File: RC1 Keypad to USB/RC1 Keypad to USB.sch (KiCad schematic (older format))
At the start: 7 parts, among them J1 RC1 Keypad Port, SW1 RESET

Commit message: Assigned keypad adapter footprints
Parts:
- A1: footprint (none) -> Arduino_Pro_Micro:Arduino_Pro_Micro
- D1, D2: renamed from D?; footprint (none) -> LEDs:LED_D5.0mm
- J1: footprint (none) -> Pin_Headers:Pin_Header_Straight_2x08_Pitch2.54mm
- R1, R2: renamed from R?; footprint (none) -> Resistors_THT:R_Axial_DIN0207_L6.3mm_D2.5mm_P10.16mm_Horizontal
- SW1: footprint (none) -> Buttons_Switches_THT:SW_PUSH_6mm
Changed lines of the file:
@@
 F 0 "J1" H 3975 3700 50  0000 C CNN
 F 1 "RC1 Keypad Port" H 4250 2500 50  0000 C CNN
-F 2 "" H 4200 3300 50  0001 C CNN
+F 2 "Pin_Headers:Pin_Header_Straight_2x08_Pitch2.54mm" H 4200 3300 50  0001 C CNN
 F 3 "" H 4200 3300 50  0001 C CNN
 	1    4250 3300
@@
 F 0 "A1" H 6350 3675 50  0000 C CNN
 F 1 "Arduino Pro Micro" V 6625 2925 50  0000 C CNN
-F 2 "" H 6575 3275 50  0001 C CNN
+F 2 "Arduino_Pro_Micro:Arduino_Pro_Micro" H 6575 3275 50  0001 C CNN
 F 3 "" H 6575 3275 50  0001 C CNN
 	1    6625 3275
@@
 F 0 "SW1" H 7375 3350 50  0000 C CNN
 F 1 "RESET" H 7375 3125 50  0000 C CNN
-F 2 "" H 7375 3225 50  0001 C CNN
+F 2 "Buttons_Switches_THT:SW_PUSH_6mm" H 7375 3225 50  0001 C CNN
 F 3 "" H 7375 3225 50  0001 C CNN
 	1    7375 3225
@@
 	6625 5200 6625 4825
 $Comp
-L R R?
+L R R2
 U 1 1 5DAC9B24
 P 7875 3225
-F 0 "R?" V 7955 3225 50  0000 C CNN
+F 0 "R2" V 7955 3225 50  0000 C CNN
 F 1 "220" V 7875 3225 50  0000 C CNN
-F 2 "" V 7805 3225 50  0001 C CNN
+F 2 "Resistors_THT:R_Axial_DIN0207_L6.3mm_D2.5mm_P10.16mm_Horizontal" V 7805 3225 50  0001 C CNN
 F 3 "" H 7875 3225 50  0001 C CNN
 	1    7875 3225
@@
 $EndComp
 $Comp
-L LED_Small D?
+L LED_Small D1
 U 1 1 5DAC9BB3
 P 7375 2700
-F 0 "D?" H 7325 2825 50  0000 L CNN
+F 0 "D1" H 7325 2825 50  0000 L CNN
 F 1 "POWER" H 7200 2600 50  0000 L CNN
-F 2 "" V 7375 2700 50  0001 C CNN
+F 2 "LEDs:LED_D5.0mm" V 7375 2700 50  0001 C CNN
 F 3 "" V 7375 2700 50  0001 C CNN
 	1    7375 2700
@@
 	7100 3625 8125 3625
 $Comp
-L LED_Small D?
+L LED_Small D2
 U 1 1 5DAC9E29
 P 8125 3475
-F 0 "D?" H 8075 3600 50  0000 L CNN
+F 0 "D2" H 8075 3600 50  0000 L CNN
 F 1 "SW_LED" H 7950 3375 50  0000 L CNN
-F 2 "" V 8125 3475 50  0001 C CNN
+F 2 "LEDs:LED_D5.0mm" V 8125 3475 50  0001 C CNN
 F 3 "" V 8125 3475 50  0001 C CNN
 	1    8125 3475
@@
 	7475 2700 7650 2700
 $Comp
-L R R?
+L R R1
 U 1 1 5DACA266
 P 6950 2700
-F 0 "R?" V 7030 2700 50  0000 C CNN
+F 0 "R1" V 7030 2700 50  0000 C CNN
 F 1 "220" V 6950 2700 50  0000 C CNN
-F 2 "" V 6880 2700 50  0001 C CNN
+F 2 "Resistors_THT:R_Axial_DIN0207_L6.3mm_D2.5mm_P10.16mm_Horizontal" V 6880 2700 50  0001 C CNN
 F 3 "" H 6950 2700 50  0001 C CNN
 	1    6950 2700

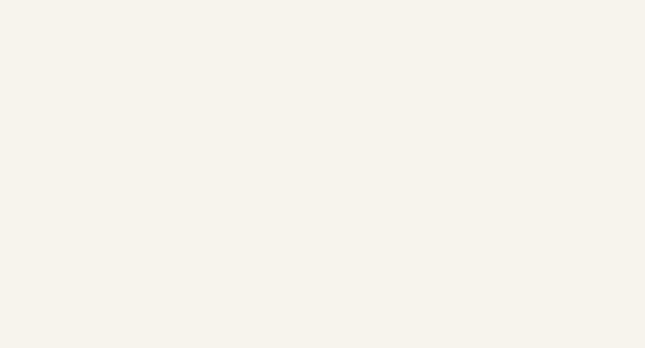
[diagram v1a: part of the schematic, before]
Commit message: Keypad to USB layout done
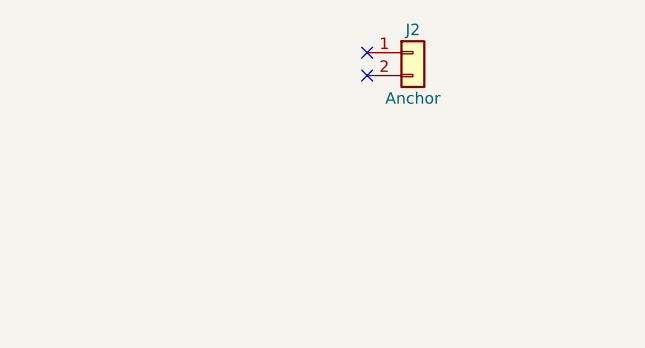
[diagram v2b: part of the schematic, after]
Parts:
- added J2: Anchor, Anchor:Pin_Header_Straight_1x02_Pitch2.54mm, symbol Conn_01x02
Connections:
- no-connect marks 6 -> 8
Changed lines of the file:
@@
 Text Notes 6975 6825 0    60   ~ 0
 With the MX keypads costing a fair bit to make, I wanted to be able to use them on the\ncomputer as well - Arduino time! The Pro Micro supports acting as an HID keyboard\nover USB so this just maps the relevant pins.
+$Comp
+L Conn_01x02 J2
+U 1 1 5DAEDC73
+P 11000 650
+F 0 "J2" H 11000 750 50  0000 C CNN
+F 1 "Anchor" H 11000 450 50  0000 C CNN
+F 2 "Anchor:Pin_Header_Straight_1x02_Pitch2.54mm" H 11000 650 50  0001 C CNN
+F 3 "" H 11000 650 50  0001 C CNN
+	1    11000 650
+	1    0    0    -1
+$EndComp
+NoConn ~ 10800 650
+NoConn ~ 10800 750
 $EndSCHEMATC
